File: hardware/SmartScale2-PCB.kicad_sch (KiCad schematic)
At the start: 55 parts, among them J1 Conn_ARM_JTAG_SWD_10, J2 USB_C_Receptacle_USB2.0_16P, J3 Conn_01x02, J4 Conn_01x04, J5 Conn_01x03_MountingPin, J6 Conn_01x04_MountingPin, Q1 MMBT4403, SW1 SW_Push_JTP-1130, U1 ESP32-C6-WROOM-1, U2 MCP73831-2-OT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

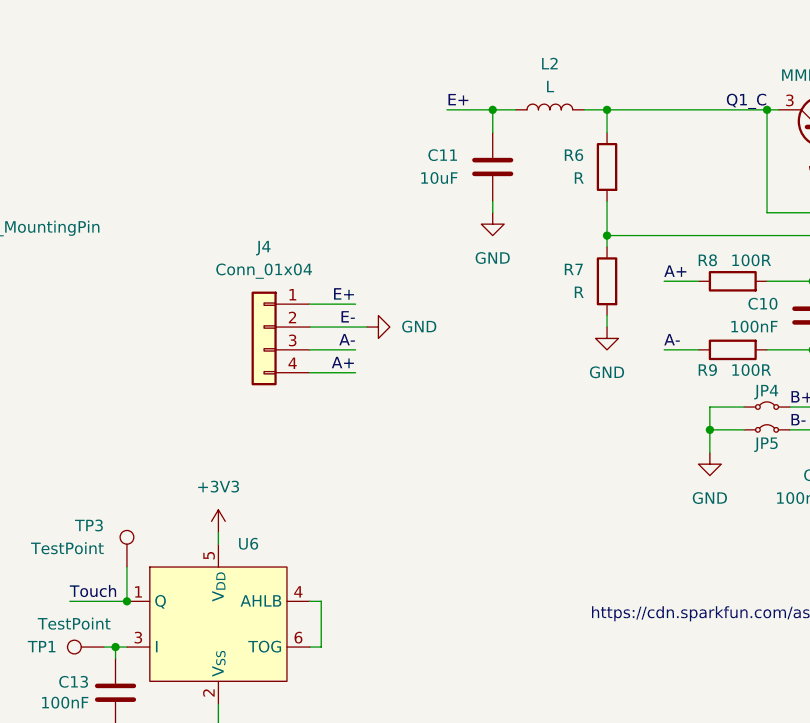
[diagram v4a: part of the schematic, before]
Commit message: Change inductor, add pin labels
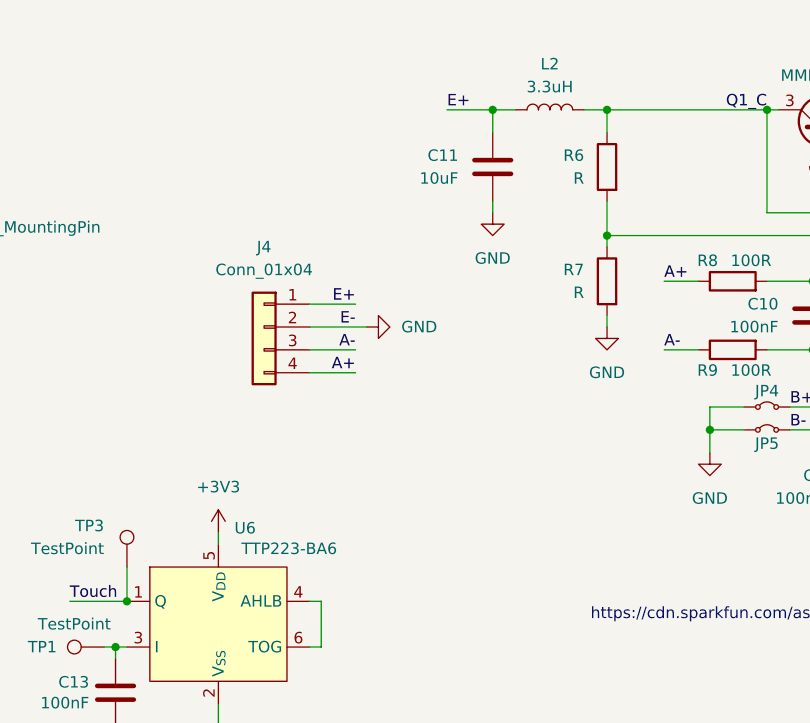
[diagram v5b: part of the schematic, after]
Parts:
- L1: footprint Inductor_SMD:L_Sunlord_SWPA5040S -> Inductor_SMD:L_Taiyo-Yuden_NR-60xx
- L2: value L -> 3.3uH
- U6: value (none) -> TTP223-BA6
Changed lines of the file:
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@@
 		(in_pos_files yes)
 		(dnp no)
-		(fields_autoplaced yes)
 		(property "Reference" "U6"
-			(at 149.4633 72.39 0)
+			(at 149.098 70.612 0)
 			(show_name no)
 			(do_not_autoplace no)
@@
 			)
 		)
-		(property "Value" ""
-			(at 147.32 81.28 0)
+		(property "Value" "TTP223-BA6"
+			(at 155.194 72.898 0)
 			(show_name no)
 			(do_not_autoplace no)
@@
 			)
 		)
-		(property "Value" "L"
+		(property "Value" "3.3uH"
 			(at 184.15 21.59 90)
 			(show_name no)
@@
 			)
 		)
-		(property "Footprint" "Inductor_SMD:L_Sunlord_SWPA5040S"
+		(property "Footprint" "Inductor_SMD:L_Taiyo-Yuden_NR-60xx"
 			(at 66.04 171.45 0)
 			(hide yes)

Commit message: Finish PCB
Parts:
- D1: value D_Zener -> BZT52C12
- J3: footprint Connector_JST:JST_ZH_B2B-ZR_1x02_P1.50mm_Vertical -> Connector_Molex:Molex_PicoBlade_53047-0210_1x02_P1.25mm_Vertical
- R1: value 12k -> 10k
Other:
- moved on the sheet: R10, R11
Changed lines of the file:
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@@
 	)
 	(junction
-		(at 172.72 154.94)
+		(at 171.45 144.78)
 		(diameter 0)
 		(color 0 0 0 0)
@@
 	(wire
 		(pts
-			(xy 172.72 154.94) (xy 172.72 156.21)
+			(xy 171.45 144.78) (xy 171.45 146.05)
 		)
 		(stroke
@@
 	(wire
 		(pts
-			(xy 172.72 154.94) (xy 182.88 154.94)
+			(xy 171.45 144.78) (xy 181.61 144.78)
 		)
 		(stroke
@@
 	(wire
 		(pts
-			(xy 172.72 144.78) (xy 172.72 146.05)
+			(xy 171.45 134.62) (xy 171.45 135.89)
 		)
 		(stroke
@@
 	(wire
 		(pts
-			(xy 172.72 153.67) (xy 172.72 154.94)
+			(xy 171.45 143.51) (xy 171.45 144.78)
 		)
 		(stroke
@@
 	)
 	(label "VBat_Div"
-		(at 182.88 154.94 180)
+		(at 181.61 144.78 180)
 		(effects
 			(font
@@
 	(symbol
 		(lib_id "power:GND")
-		(at 172.72 163.83 0)
+		(at 171.45 153.67 0)
 		(unit 1)
 		(body_style 1)
@@
 		(fields_autoplaced yes)
 		(property "Reference" "#PWR022"
-			(at 172.72 170.18 0)
+			(at 171.45 160.02 0)
 			(hide yes)
 			(show_name no)
@@
 		)
 		(property "Value" "GND"
-			(at 172.72 168.91 0)
+			(at 171.45 158.75 0)
 			(show_name no)
 			(do_not_autoplace no)
@@
 		)
 		(property "Footprint" ""
-			(at 172.72 163.83 0)
+			(at 171.45 153.67 0)
 			(hide yes)
 			(show_name no)
@@
 		)
 		(property "Datasheet" ""
-			(at 172.72 163.83 0)
+			(at 171.45 153.67 0)
 			(hide yes)
 			(show_name no)
@@
 		)
 		(property "Description" "Power symbol creates a global label with name \"GND\" , ground"
-			(at 172.72 163.83 0)
+			(at 171.45 153.67 0)
 			(hide yes)
 			(show_name no)
@@
 	(symbol
 		(lib_id "Device:R")
-		(at 172.72 160.02 0)
+		(at 171.45 149.86 0)
 		(mirror y)
 		(unit 1)
@@
 		(dnp yes)
 		(property "Reference" "R11"
-			(at 170.18 158.7499 0)
+			(at 168.91 148.5899 0)
 			(show_name no)
 			(do_not_autoplace no)
@@
 		)
 		(property "Value" "10k"
-			(at 170.18 161.2899 0)
+			(at 168.91 151.1299 0)
 			(show_name no)
 			(do_not_autoplace no)
@@
 		)
 		(property "Footprint" "Resistor_SMD:R_0805_2012Metric_Pad1.20x1.40mm_HandSolder"
-			(at 174.498 160.02 90)
+			(at 173.228 149.86 90)
 			(hide yes)
 			(show_name no)
@@
 		)
 		(property "Datasheet" ""
-			(at 172.72 160.02 0)
+			(at 171.45 149.86 0)
 			(hide yes)
 			(show_name no)
@@
 		)
 		(property "Description" "Resistor"
-			(at 172.72 160.02 0)
+			(at 171.45 149.86 0)
 			(hide yes)
 			(show_name no)
@@
 			)
 		)
-		(property "Footprint" "Connector_JST:JST_ZH_B2B-ZR_1x02_P1.50mm_Vertical"
+		(property "Footprint" "Connector_Molex:Molex_PicoBlade_53047-0210_1x02_P1.25mm_Vertical"
 			(at 149.86 176.53 0)
 			(hide yes)
@@
 			)
 		)
-		(property "Value" "D_Zener"
+		(property "Value" "BZT52C12"
 			(at 237.49 107.9499 90)
 			(show_name no)
@@
 	(symbol
 		(lib_id "Device:R")
-		(at 172.72 149.86 0)
+		(at 171.45 139.7 0)
 		(mirror y)
 		(unit 1)
@@
 		(dnp yes)
 		(property "Reference" "R10"
-			(at 170.18 148.5899 0)
+			(at 168.91 138.4299 0)
 			(show_name no)
 			(do_not_autoplace no)
@@
 		)
 		(property "Value" "33k"
-			(at 170.18 151.1299 0)
+			(at 168.91 140.9699 0)
 			(show_name no)
 			(do_not_autoplace no)
@@
 		)
 		(property "Footprint" "Resistor_SMD:R_0805_2012Metric_Pad1.20x1.40mm_HandSolder"
-			(at 174.498 149.86 90)
+			(at 173.228 139.7 90)
 			(hide yes)
 			(show_name no)
@@
 		)
 		(property "Datasheet" ""
-			(at 172.72 149.86 0)
+			(at 171.45 139.7 0)
 			(hide yes)
 			(show_name no)
@@
 		)
 		(property "Description" "Resistor"
-			(at 172.72 149.86 0)
+			(at 171.45 139.7 0)
 			(hide yes)
 			(show_name no)
@@
 	(symbol
 		(lib_id "power:+BATT")
-		(at 172.72 144.78 0)
+		(at 171.45 134.62 0)
 		(unit 1)
 		(body_style 1)
@@
 		(fields_autoplaced yes)
 		(property "Reference" "#PWR032"
-			(at 172.72 148.59 0)
+			(at 171.45 138.43 0)
 			(hide yes)
 			(show_name no)
@@
 		)
 		(property "Value" "+BATT"
-			(at 172.72 139.7 0)
+			(at 171.45 129.54 0)
 			(show_name no)
 			(do_not_autoplace no)
@@
 		)
 		(property "Footprint" ""
-			(at 172.72 144.78 0)
+			(at 171.45 134.62 0)
 			(hide yes)
 			(show_name no)
@@
 		)
 		(property "Datasheet" ""
-			(at 172.72 144.78 0)
+			(at 171.45 134.62 0)
 			(hide yes)
 			(show_name no)
@@
 		)
 		(property "Description" "Power symbol creates a global label with name \"+BATT\""
-			(at 172.72 144.78 0)
+			(at 171.45 134.62 0)
 			(hide yes)
 			(show_name no)
@@
 			)
 		)
-		(property "Value" "12k"
+		(property "Value" "10k"
 			(at 93.218 123.063 0)
 			(show_name no)

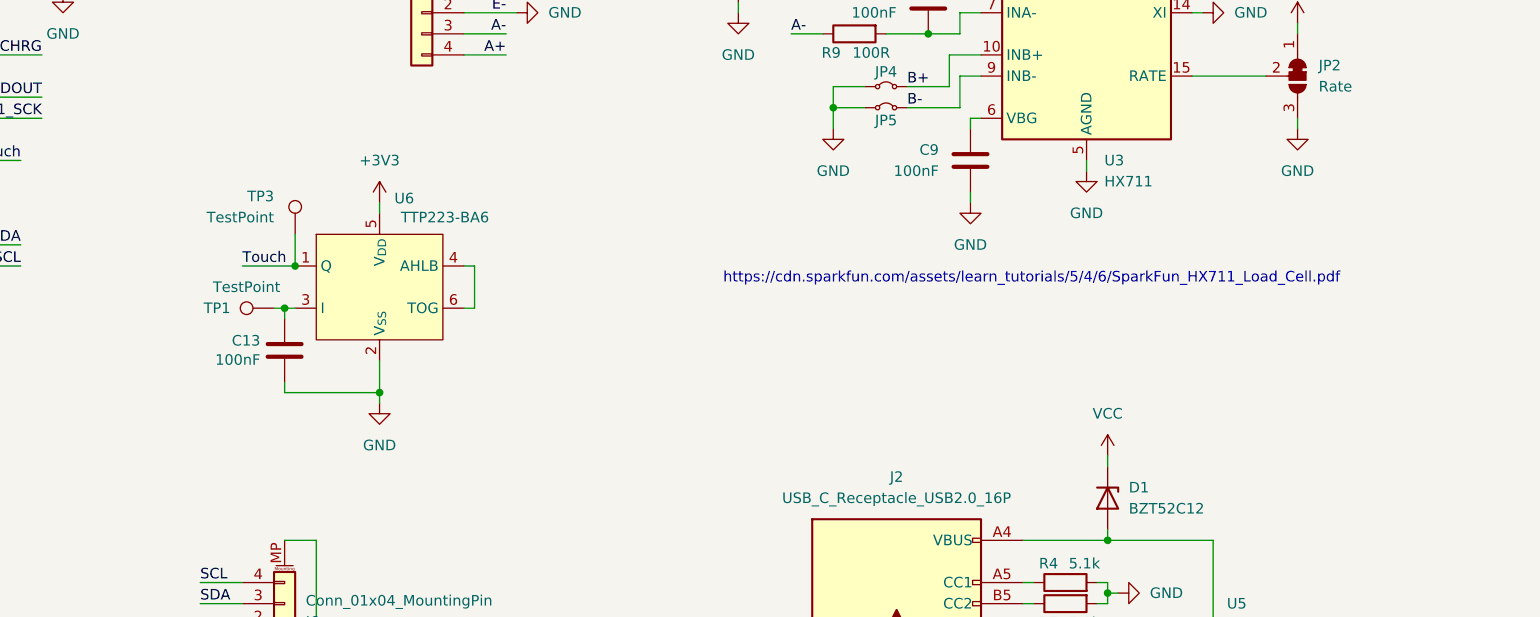
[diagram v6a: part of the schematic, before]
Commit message: Add jumpers for touch ic pins, render ui on display
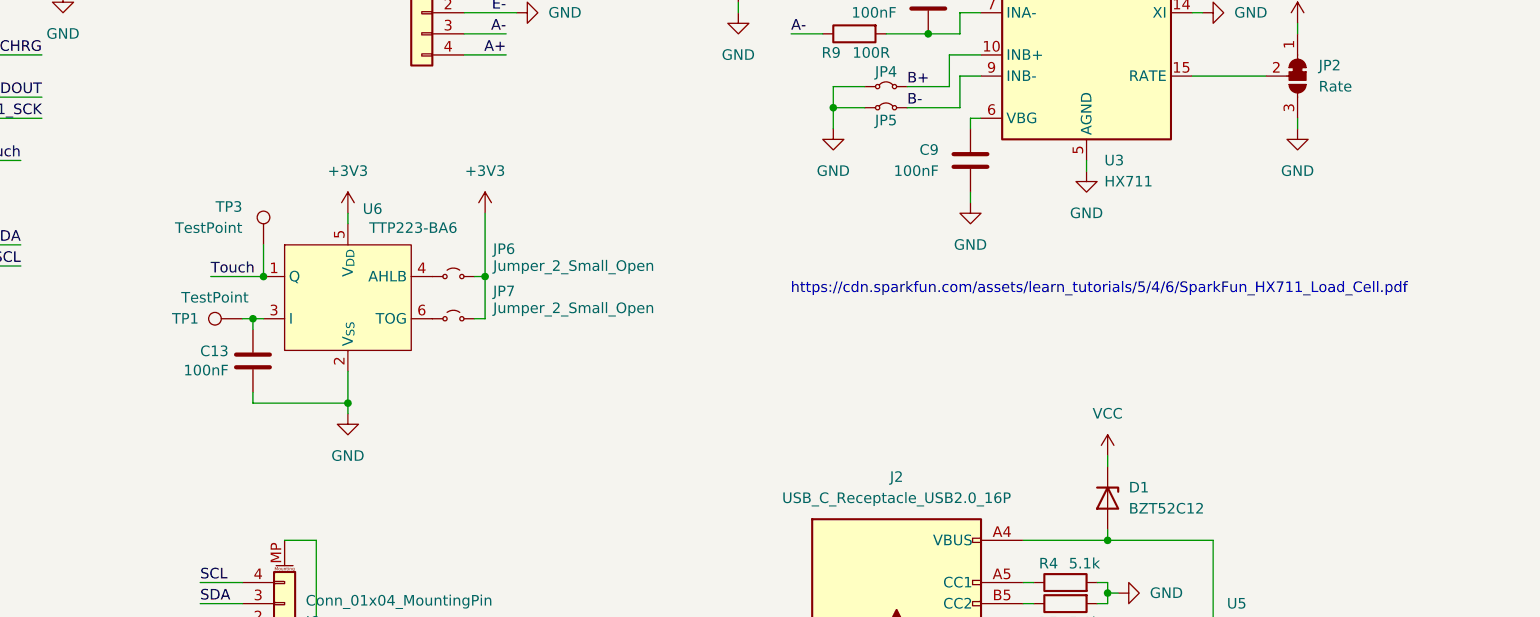
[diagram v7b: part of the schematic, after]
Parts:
- added JP6, JP7: Jumper_2_Small_Open, Jumper:SolderJumper-2_P1.3mm_Open_RoundedPad1.0x1.5mm, symbol Jumper:Jumper_2_Small_Open
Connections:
- net +3V3: now also JP6.2 (B), JP7.2 (B)
- net at U6.4 (AHLB): now also JP6.1 (A); no longer U6.6 (TOG)
- new net: JP7.1 (A), U6.6 (TOG)
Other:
- moved on the sheet: C13, TP1, TP3, U6
